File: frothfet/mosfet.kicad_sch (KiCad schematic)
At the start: 27 parts, among them Q1 BSC010N04LS, U2 LM74502H, U3 INA226, U4 LM75BD

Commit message: updated bom and checked placement
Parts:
- F1, F2, F3: value Conn_01x01_Pin -> T508; LCSC C41371870 -> C41355742
- Q1: LCSC (none) -> C501508
- R10, R6: LCSC (none) -> C25804
- R8, R9: LCSC (none) -> C844794
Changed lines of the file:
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@@
 			)
 		)
-		(property "LCSC" ""
+		(property "LCSC" "C844794"
 			(at 130.81 111.76 0)
 			(effects
@@
 			)
 		)
-		(property "LCSC" ""
+		(property "LCSC" "C25804"
 			(at 52.07 69.85 0)
 			(effects
@@
 			)
 		)
-		(property "LCSC" ""
+		(property "LCSC" "C844794"
 			(at 130.81 119.38 0)
 			(effects
@@
 			)
 		)
-		(property "Value" "Conn_01x01_Pin"
+		(property "Value" "T508"
 			(at 176.53 55.2451 90)
 			(effects
@@
 			)
 		)
-		(property "LCSC" "C41371870"
+		(property "LCSC" "C41355742"
 			(at 177.8 57.15 90)
 			(effects
@@
 			)
 		)
-		(property "Value" "Conn_01x01_Pin"
+		(property "Value" "T508"
 			(at 179.7049 62.23 90)
 			(effects
@@
 			)
 		)
-		(property "LCSC" "C41371870"
+		(property "LCSC" "C41355742"
 			(at 177.8 63.5 0)
 			(effects
@@
 			)
 		)
+		(property "LCSC" "C501508"
+			(at 120.65 59.69 0)
+			(effects
+				(font
+					(size 1.27 1.27)
+				)
+				(hide yes)
+			)
+		)
 		(pin "2"
 		)
@@
 			)
 		)
-		(property "LCSC" ""
+		(property "LCSC" "C25804"
 			(at 182.88 113.03 0)
 			(effects
@@
 			)
 		)
-		(property "Value" "Conn_01x01_Pin"
+		(property "Value" "T508"
 			(at 179.07 71.7549 90)
 			(effects
@@
 			)
 		)
-		(property "LCSC" "C41371870"
+		(property "LCSC" "C41355742"
 			(at 177.8 69.85 90)
 			(effects

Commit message: finished vias, added a bunch of test points
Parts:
- added TP49, TP50, TP51, TP52, TP81: TestPoint, TestPoint:TestPoint_Pad_D1.5mm, symbol Connector:TestPoint
- TP3, TP4, TP5, TP6: symbol Connector:TestPoint -> Connector:TestPoint_Probe; now in the parts list
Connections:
- net GND: now also TP81.1
- net LOAD: now also TP52.1
- net LOAD_SWITCHED: now also TP51.1
- net LOAD_VSS: now also TP50.1
- net at D1.1 (K), Q1.2 (G), TP3.1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: now also TP49.1

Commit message: bom and placement looking good.
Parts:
- added F34: ATC Fuse Bypass, yarrboard:ATC Bypass Fuse, symbol yarrboard:ATC Fuse Bypass
- C2, C4, C5, C6, C7: LCSC (none) -> C14663
- C3: LCSC (none) -> C21120
- TP3: symbol Connector:TestPoint_Probe -> yarrboard:TestPoint_Probe; now left out of the parts list
- TP4, TP5, TP6: footprint TestPoint:TestPoint_THTPad_D1.5mm_Drill0.7mm -> TestPoint:TestPoint_THTPad_D1.0mm_Drill0.5mm; symbol Connector:TestPoint_Probe -> yarrboard:TestPoint_Probe; now left out of the parts list
- TP49, TP50, TP51, TP52, TP81: symbol Connector:TestPoint -> yarrboard:TestPoint; now left out of the parts list
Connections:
- net +24V: now also F34.2
- net LOAD_SWITCHED: now also F34.3
- net LOAD_VSS: now also F34.1
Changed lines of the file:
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@@
 	)
 	(junction
+		(at 186.69 63.5)
+		(diameter 0)
+		(color 0 0 0 0)
+	)
+	(junction
 		(at 157.48 125.73)
 		(diameter 0)
@@
 	)
 	(junction
+		(at 177.8 78.74)
+		(diameter 0)
+		(color 0 0 0 0)
+	)
+	(junction
 		(at 123.19 46.99)
 		(diameter 0)
@@
 	)
 	(junction
+		(at 177.8 46.99)
+		(diameter 0)
+		(color 0 0 0 0)
+	)
+	(junction
 		(at 137.16 111.76)
 		(diameter 0)
@@
 	(wire
 		(pts
+			(xy 194.31 72.39) (xy 194.31 78.74)
+		)
+		(stroke
+			(width 0)
+			(type default)
+		)
+	)
+	(wire
+		(pts
 			(xy 69.85 83.82) (xy 58.42 83.82)
 		)
@@
 	(wire
 		(pts
+			(xy 186.69 63.5) (xy 191.77 63.5)
+		)
+		(stroke
+			(width 0)
+			(type default)
+		)
+	)
+	(wire
+		(pts
 			(xy 123.19 50.8) (xy 123.19 54.61)
 		)
@@
 	(wire
 		(pts
+			(xy 194.31 46.99) (xy 177.8 46.99)
+		)
+		(stroke
+			(width 0)
+			(type default)
+		)
+	)
+	(wire
+		(pts
+			(xy 194.31 78.74) (xy 177.8 78.74)
+		)
+		(stroke
+			(width 0)
+			(type default)
+		)
+	)
+	(wire
+		(pts
 			(xy 186.69 59.69) (xy 186.69 63.5)
 		)
@@
 	(wire
 		(pts
+			(xy 194.31 54.61) (xy 194.31 46.99)
+		)
+		(stroke
+			(width 0)
+			(type default)
+		)
+	)
+	(wire
+		(pts
 			(xy 38.1 83.82) (xy 58.42 83.82)
 		)
@@
 			)
 		)
-		(property "LCSC" ""
+		(property "LCSC" "C14663"
 			(at 195.58 113.03 0)
 			(effects
@@
 	)
 	(symbol
-		(lib_id "Connector:TestPoint_Probe")
+		(lib_id "yarrboard:TestPoint_Probe")
 		(at 121.92 85.09 90)
 		(unit 1)
 		(exclude_from_sim no)
-		(in_bom yes)
+		(in_bom no)
 		(on_board yes)
 		(dnp no)
@@
 			)
 		)
-		(property "Footprint" "TestPoint:TestPoint_THTPad_D1.5mm_Drill0.7mm"
+		(property "Footprint" "TestPoint:TestPoint_THTPad_D1.0mm_Drill0.5mm"
 			(at 121.92 80.01 0)
 			(effects
@@
 	)
 	(symbol
-		(lib_id "Connector:TestPoint")
+		(lib_id "yarrboard:TestPoint")
 		(at 123.19 130.81 270)
 		(unit 1)
 		(exclude_from_sim no)
-		(in_bom yes)
+		(in_bom no)
 		(on_board yes)
 		(dnp no)
@@
 	)
 	(symbol
-		(lib_id "Connector:TestPoint_Probe")
+		(lib_id "yarrboard:TestPoint_Probe")
 		(at 121.92 50.8 90)
 		(unit 1)
 		(exclude_from_sim no)
-		(in_bom yes)
+		(in_bom no)
 		(on_board yes)
 		(dnp no)
@@
 			)
 		)
-		(property "Footprint" "TestPoint:TestPoint_THTPad_D1.5mm_Drill0.7mm"
+		(property "Footprint" "TestPoint:TestPoint_THTPad_D1.0mm_Drill0.5mm"
 			(at 121.92 45.72 0)
 			(effects
@@
 	)
 	(symbol
+		(lib_id "yarrboard:ATC Fuse Bypass")
+		(at 194.31 63.5 0)
+		(mirror y)
+		(unit 1)
+		(exclude_from_sim no)
+		(in_bom yes)
+		(on_board no)
+		(dnp yes)
+		(property "Reference" "F34"
+			(at 196.85 62.2299 0)
+			(effects
+				(font
+					(size 1.27 1.27)
+				)
+				(justify right)
+			)
+		)
+		(property "Value" "ATC Fuse Bypass"
+			(at 196.85 64.7699 0)
+			(effects
+				(font
+					(size 1.27 1.27)
+				)
+				(justify right)
+				(hide yes)
+			)
+		)
+		(property "Footprint" "yarrboard:ATC Bypass Fuse"
+			(at 196.088 58.42 90)
+			(effects
+				(font
+					(size 1.27 1.27)
+				)
+				(hide yes)
+			)
+		)
+		(property "Datasheet" "~"
+			(at 194.31 58.42 0)
+			(effects
+				(font
+					(size 1.27 1.27)
+				)
+				(hide yes)
+			)
+		)
+		(property "Description" "Fuse"
+			(at 194.31 63.5 0)
+			(effects
+				(font
+					(size 1.27 1.27)
+				)
+				(hide yes)
+			)
+		)
+		(pin "1"
+		)
+		(pin "3"
+		)
+		(pin "2"
+		)
+		(instances
+			(project ""
+				(path "/c83c6236-96e9-46ad-9d7a-9e2efa4a7966/0eec6767-666b-42c0-ba36-2a83c9caeade"
+					(reference "F34")
+					(unit 1)
+				)
+				(path "/c83c6236-96e9-46ad-9d7a-9e2efa4a7966/1e692482-a022-407a-8cb5-d9a3b23521a6"
+					(reference "F36")
+					(unit 1)
+				)
+				(path "/c83c6236-96e9-46ad-9d7a-9e2efa4a7966/424e7b24-5644-46f2-85bb-1e459a343705"
+					(reference "F39")
+					(unit 1)
+				)
+				(path "/c83c6236-96e9-46ad-9d7a-9e2efa4a7966/4c1df725-56ca-4be4-8107-a39054acbca4"
+					(reference "F40")
+					(unit 1)
+				)
+				(path "/c83c6236-96e9-46ad-9d7a-9e2efa4a7966/5952e660-2bb6-45cf-b9ea-f7a7c2d0954e"
+					(reference "F37")
+					(unit 1)
+				)
+				(path "/c83c6236-96e9-46ad-9d7a-9e2efa4a7966/772d44f5-8758-48db-a140-72ed8e75e88c"
+					(reference "F38")
+					(unit 1)
+				)
+				(path "/c83c6236-96e9-46ad-9d7a-9e2efa4a7966/a8a81147-5613-4820-beb3-a7ca76d0db8e"
+					(reference "F41")
+					(unit 1)
+				)
+				(path "/c83c6236-96e9-46ad-9d7a-9e2efa4a7966/ccdb1c25-8d0f-4f30-ab70-bbc1ecf3f6f7"
+					(reference "F35")
+					(unit 1)
+				)
+			)
+		)
+	)
+	(symbol
 		(lib_id "power:GND")
 		(at 58.42 85.09 0)
@@
 	)
 	(symbol
-		(lib_id "Connector:TestPoint")
+		(lib_id "yarrboard:TestPoint")
 		(at 123.19 50.8 270)
 		(unit 1)
 		(exclude_from_sim no)
-		(in_bom yes)
+		(in_bom no)
 		(on_board yes)
 		(dnp no)
@@
 			)
 		)
-		(property "LCSC" ""
+		(property "LCSC" "C14663"
 			(at 137.16 115.57 0)
 			(effects
@@
 	)
 	(symbol
-		(lib_id "Connector:TestPoint")
+		(lib_id "yarrboard:TestPoint")
 		(at 123.19 149.86 180)
 		(unit 1)
 		(exclude_from_sim no)
-		(in_bom yes)
+		(in_bom no)
 		(on_board yes)
 		(dnp no)
@@
 			)
 		)
-		(property "LCSC" ""
+		(property "LCSC" "C14663"
 			(at 259.08 59.69 90)
 			(effects
@@
 			)
 		)
-		(property "LCSC" ""
+		(property "LCSC" "C14663"
 			(at 38.1 63.5 0)
 			(effects
@@
 			)
 		)
-		(property "LCSC" ""
+		(property "LCSC" "C14663"
 			(at 214.63 114.3 0)
 			(effects
@@
 	)
 	(symbol
-		(lib_id "Connector:TestPoint")
+		(lib_id "yarrboard:TestPoint")
 		(at 123.19 85.09 270)
 		(mirror x)
 		(unit 1)
 		(exclude_from_sim no)
-		(in_bom yes)
+		(in_bom no)
 		(on_board yes)
 		(dnp no)
@@
 			)
 		)
-		(property "LCSC" ""
+		(property "LCSC" " C21120"
 			(at 59.69 63.5 0)
 			(effects
@@
 	)
 	(symbol
-		(lib_id "Connector:TestPoint")
+		(lib_id "yarrboard:TestPoint")
 		(at 106.68 59.69 0)
 		(unit 1)
 		(exclude_from_sim no)
-		(in_bom yes)
+		(in_bom no)
 		(on_board yes)
 		(dnp no)
@@
 	)
 	(symbol
-		(lib_id "Connector:TestPoint_Probe")
+		(lib_id "yarrboard:TestPoint_Probe")
 		(at 99.06 58.42 0)
 		(unit 1)
 		(exclude_from_sim no)
-		(in_bom yes)
+		(in_bom no)
 		(on_board yes)
 		(dnp no)
@@
 	)
 	(symbol
-		(lib_id "Connector:TestPoint_Probe")
+		(lib_id "yarrboard:TestPoint_Probe")
 		(at 121.92 130.81 90)
 		(unit 1)
 		(exclude_from_sim no)
-		(in_bom yes)
+		(in_bom no)
 		(on_board yes)
 		(dnp no)
@@
 			)
 		)
-		(property "Footprint" "TestPoint:TestPoint_THTPad_D1.5mm_Drill0.7mm"
+		(property "Footprint" "TestPoint:TestPoint_THTPad_D1.0mm_Drill0.5mm"
 			(at 121.92 125.73 0)
 			(effects

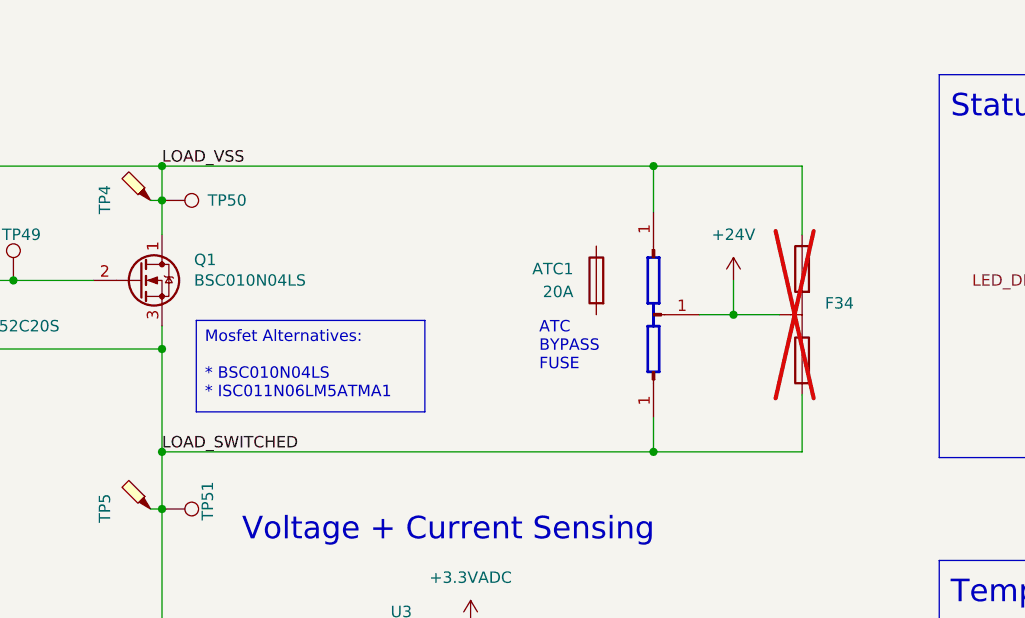
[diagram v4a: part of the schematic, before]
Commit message: switch back to T507 fuse holder is complete
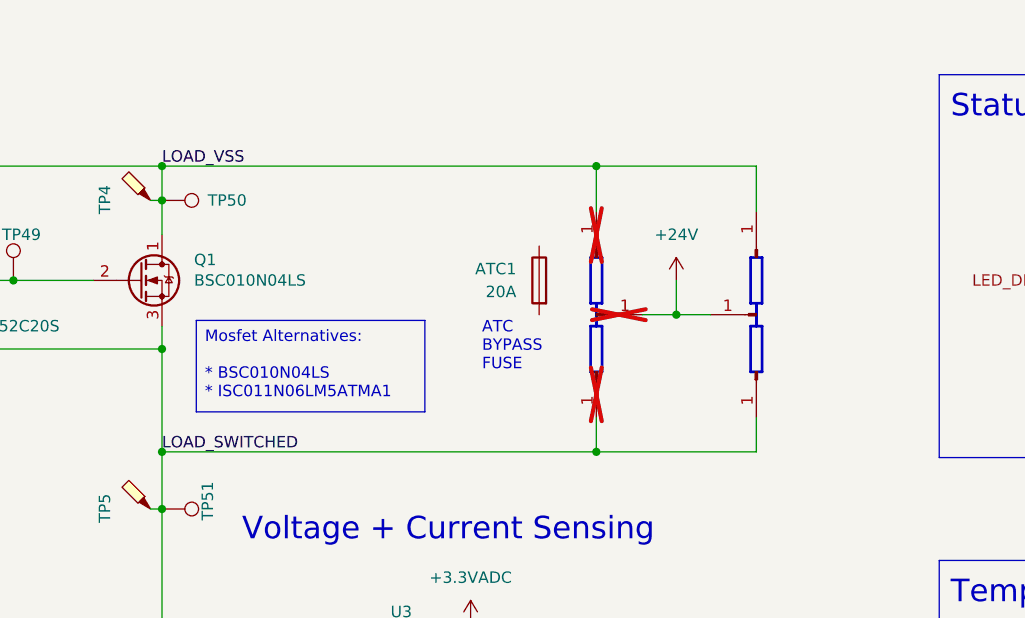
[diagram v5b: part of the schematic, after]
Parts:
- removed F34: ATC Fuse Bypass, yarrboard:ATC Bypass Fuse, symbol yarrboard:ATC Fuse Bypass
- added F42, F43, F44: T508, yarrboard:XFCN T507, symbol Connector:Conn_01x01_Pin
- F1, F2, F3: now not fitted
- TP3, TP4, TP5, TP6: footprint TestPoint:TestPoint_THTPad_D1.0mm_Drill0.5mm -> yarrboard:TestPoint_THTPad_D1.0mm_Drill0.5mm
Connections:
- net +24V: now also F43.1 (Pin_1)
- net LOAD_SWITCHED: now also F44.1 (Pin_1)
- net LOAD_VSS: now also F42.1 (Pin_1)
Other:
- moved on the sheet: ATC1

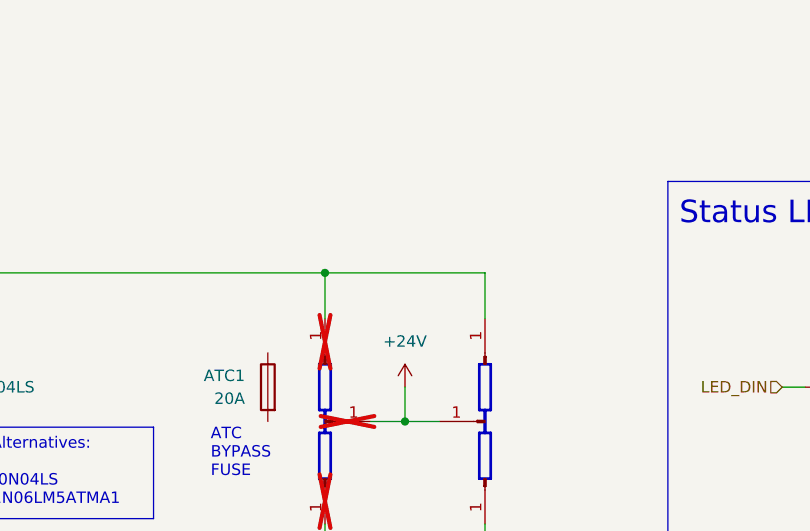
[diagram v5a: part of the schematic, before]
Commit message: a few routing tweaks, removed DNP on pin headers for uart0
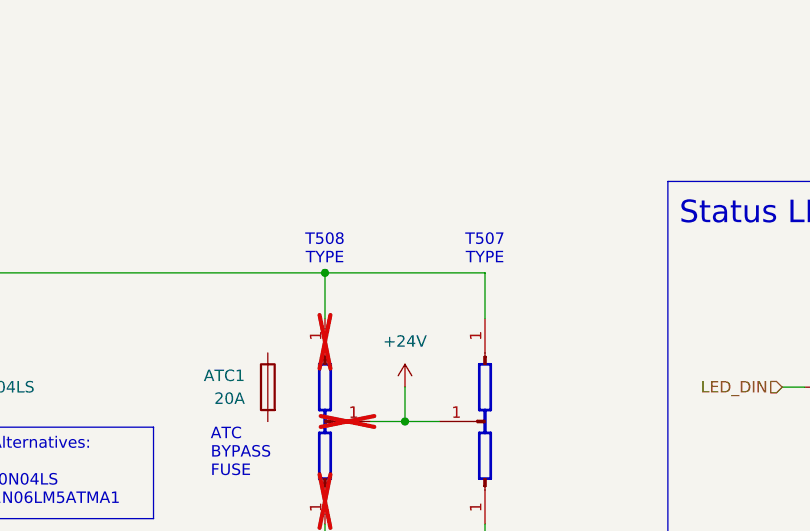
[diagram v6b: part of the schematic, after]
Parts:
- F42, F43, F44: LCSC C41355742 -> C41371870
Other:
- note added: "T507 TYPE"
- note added: "T508 TYPE"
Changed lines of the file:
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@@
 		)
 	)
+	(text "T507\nTYPE"
+		(exclude_from_sim no)
+		(at 189.23 44.45 0)
+		(effects
+			(font
+				(size 1.27 1.27)
+			)
+		)
+	)
 	(text "Temperature Sensing"
 		(exclude_from_sim no)
@@
 		)
 	)
+	(text "T508\nTYPE"
+		(exclude_from_sim no)
+		(at 171.45 44.45 0)
+		(effects
+			(font
+				(size 1.27 1.27)
+			)
+		)
+	)
 	(text "Status LED"
 		(exclude_from_sim no)
@@
 			)
 		)
-		(property "LCSC" "C41355742"
+		(property "LCSC" "C41371870"
 			(at 189.23 63.5 0)
 			(effects
@@
 			)
 		)
-		(property "LCSC" "C41355742"
+		(property "LCSC" "C41371870"
 			(at 189.23 57.15 90)
 			(effects
@@
 			)
 		)
-		(property "LCSC" "C41355742"
+		(property "LCSC" "C41371870"
 			(at 189.23 69.85 90)
 			(effects

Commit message: added fuse p/n and drawing
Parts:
- ATC1: LCSC (none) -> C142685
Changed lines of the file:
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@@
+			)
+		)
+		(property "LCSC" "C142685"
+			(at 165.1 59.69 0)
+			(effects
+				(font
+					(size 1.27 1.27)
+				)
+				(hide yes)
 			)
 		)

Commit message: final bom tweaks for manufacturing
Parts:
- F42, F43, F44: value T508 -> C41371870; Rotation Offset (none) -> 90
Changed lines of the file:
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@@
 			)
 		)
-		(property "Value" "T508"
+		(property "Value" "C41371870"
 			(at 187.3251 62.23 90)
 			(effects
@@
 		)
 		(property "LCSC" "C41371870"
+			(at 189.23 63.5 0)
+			(effects
+				(font
+					(size 1.27 1.27)
+				)
+				(hide yes)
+			)
+		)
+		(property "Rotation Offset" "90"
 			(at 189.23 63.5 0)
 			(effects
@@
 			)
 		)
-		(property "Value" "T508"
+		(property "Value" "C41371870"
 			(at 190.5 55.2451 90)
 			(effects
@@
 		)
 		(property "LCSC" "C41371870"
+			(at 189.23 57.15 90)
+			(effects
+				(font
+					(size 1.27 1.27)
+				)
+				(hide yes)
+			)
+		)
+		(property "Rotation Offset" "90"
 			(at 189.23 57.15 90)
 			(effects
@@
 			)
 		)
-		(property "Value" "T508"
+		(property "Value" "C41371870"
 			(at 187.96 71.7549 90)
 			(effects
@@
 			(at 189.23 69.85 90)
 			(effects
+				(font
+					(size 1.27 1.27)
+				)
+				(hide yes)
+			)
+		)
+		(property "Rotation Offset" "90"
+			(at 189.23 69.85 90)
+			(effects
